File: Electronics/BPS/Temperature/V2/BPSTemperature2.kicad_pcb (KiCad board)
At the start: 2 copper layers, 75 x 65 mm, 81 parts, among them J1 Conn_02x10_Counter_Clockwise, J2 Logic Analyzer, J3 Conn_02x06_Counter_Clockwise, J4 Conn_02x06_Counter_Clockwise, J5 Conn_01x02, SW1 SW_DIP_x06, U1 LTC2983

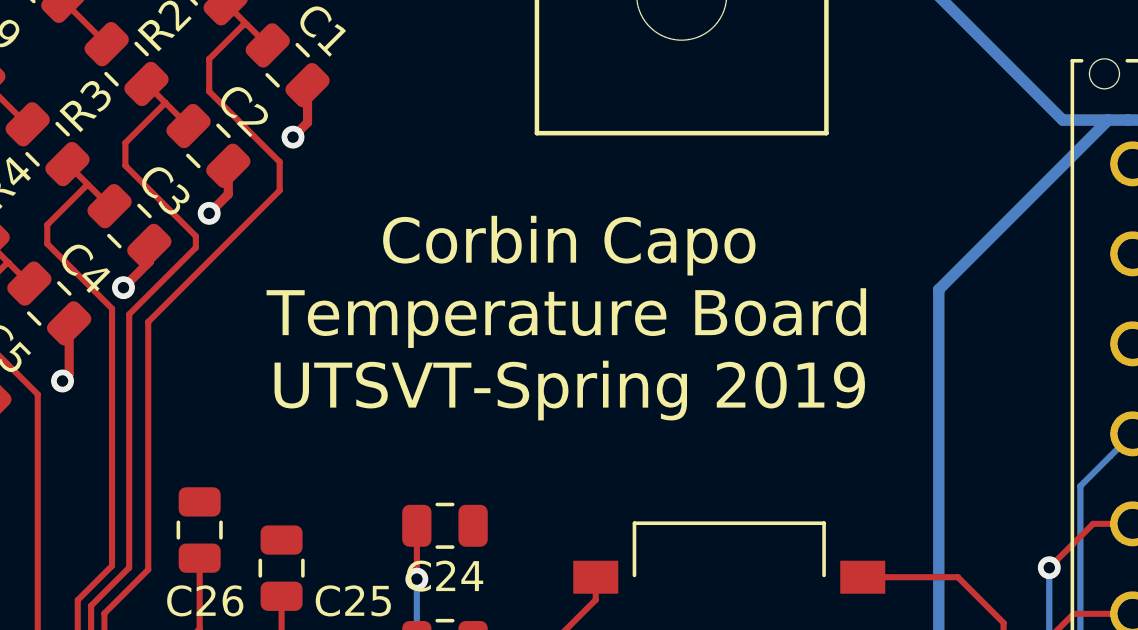
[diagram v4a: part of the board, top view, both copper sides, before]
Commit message: Added names to temperature board for BPS
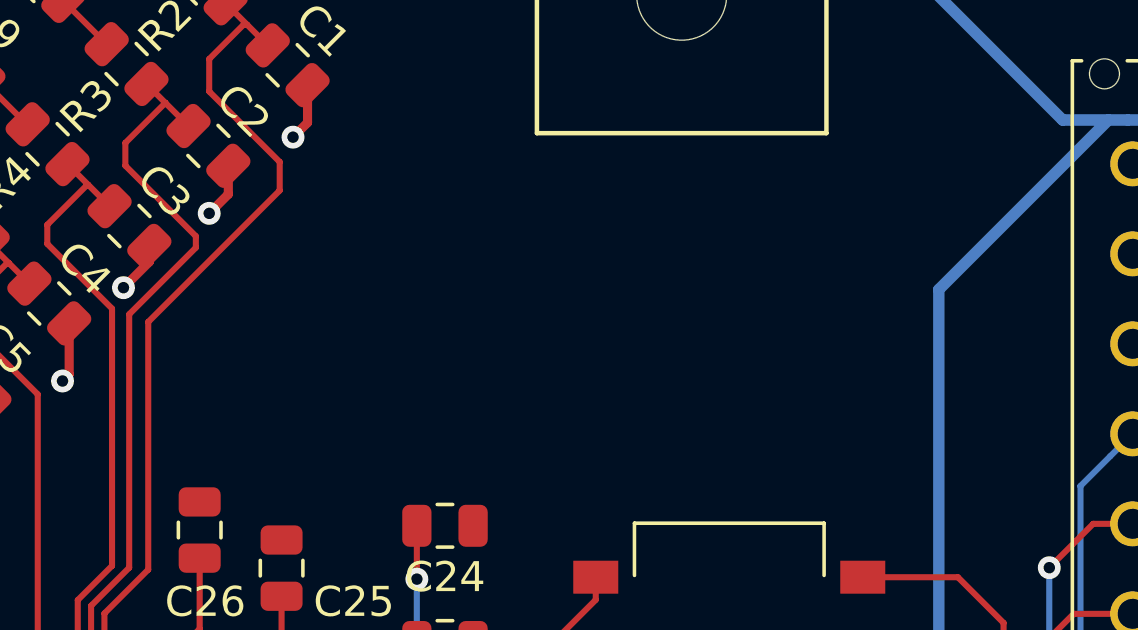
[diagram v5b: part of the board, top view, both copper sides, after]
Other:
- board text added: "Monolo Alvarez Chase Block Corbin Capo Richard Li Garrett Wong Sijin Woo Temperature Board UTSVT-Spring 2019"
- board text removed: "Corbin Capo Temperature Board UTSVT-Spring 2019"
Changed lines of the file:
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@@
     (effects (font (size 1.5 1.5) (thickness 0.3)))
   )
-  (gr_text "Corbin Capo\nTemperature Board\nUTSVT-Spring 2019" (at 109.601 86.5505) (layer F.SilkS)
-    (effects (font (size 1.5 1.5) (thickness 0.3)))
+  (gr_text "Monolo Alvarez\n\nChase Block\n\nCorbin Capo\n\nRichard Li\n\nGarrett Wong\n\nSijin Woo\nTemperature Board\nUTSVT-Spring 2019" (at 101.981 82.296) (layer B.SilkS)
+    (effects (font (size 0.738 0.738) (thickness 0.1845)) (justify mirror))
   )
   (gr_line (start 135 70) (end 60 70) (layer Edge.Cuts) (width 0.1))

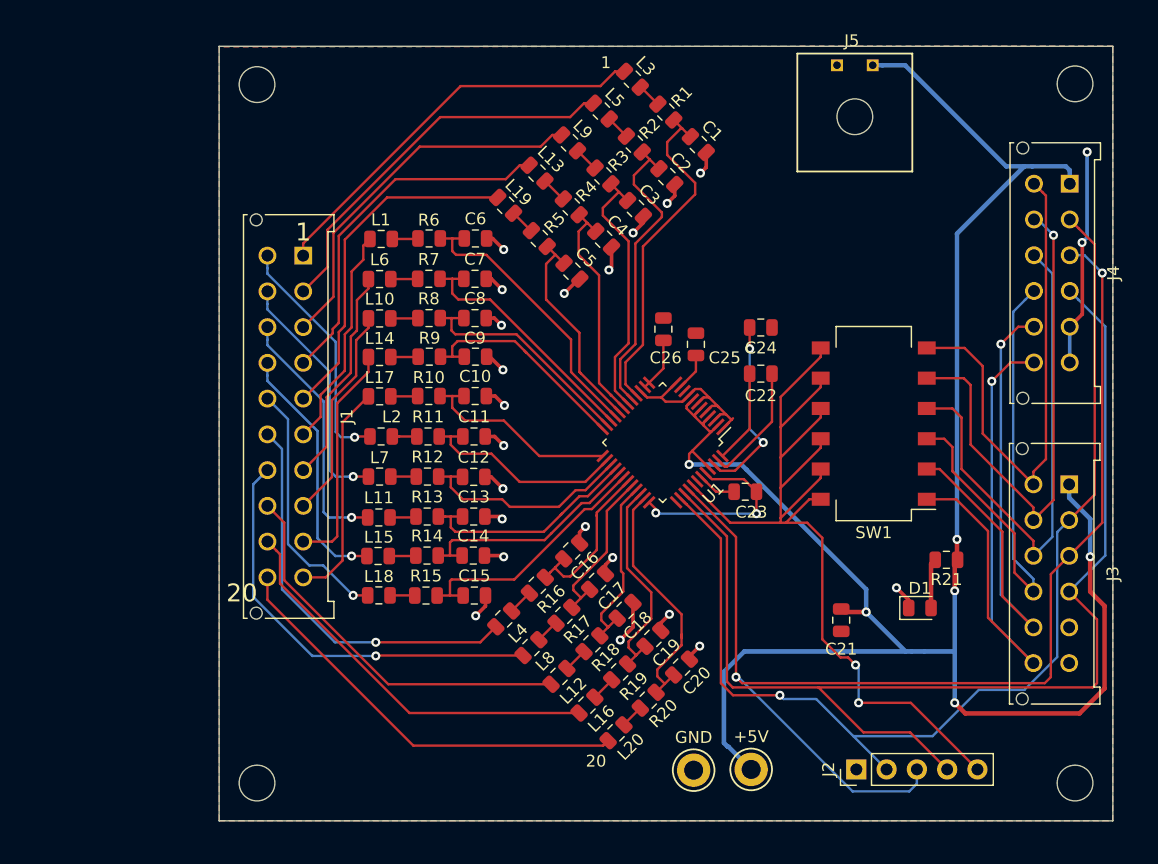
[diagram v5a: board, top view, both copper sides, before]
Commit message: Modified footprint for connector
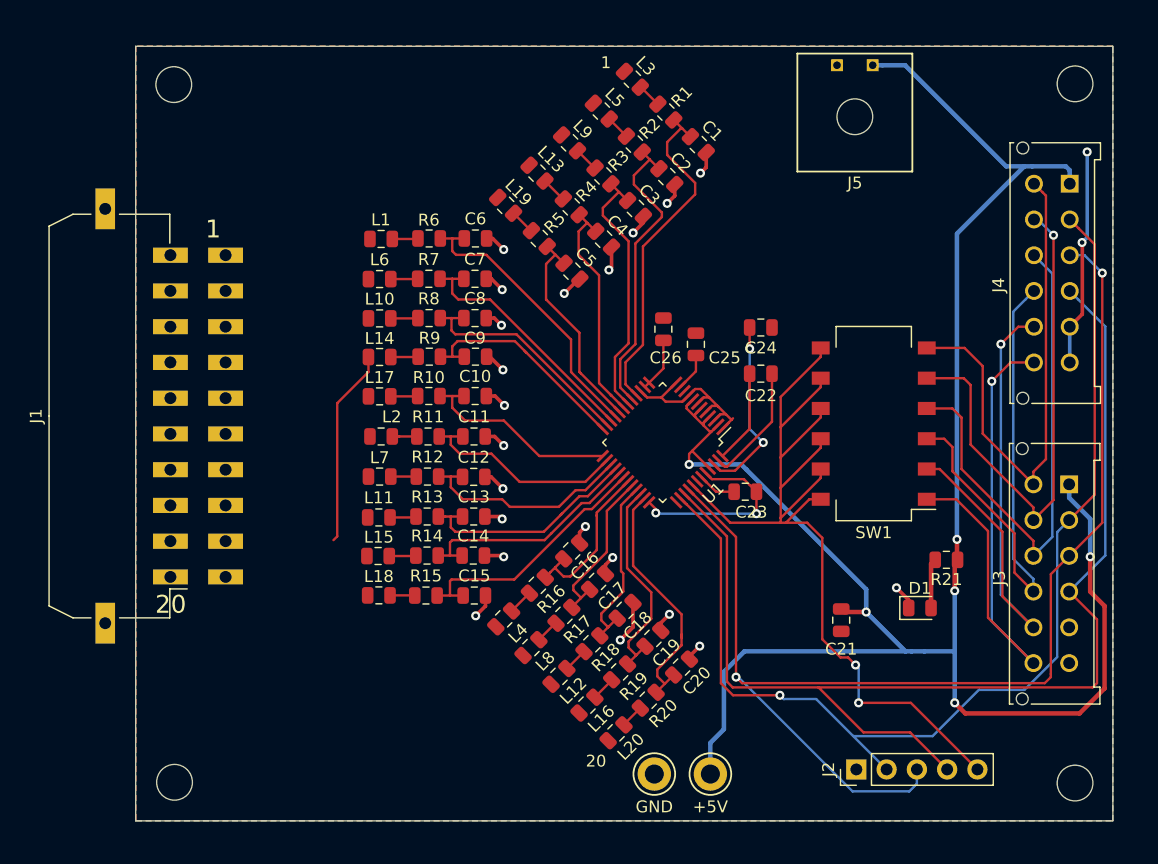
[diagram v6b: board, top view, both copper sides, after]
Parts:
- J1: footprint Connector_Molex:Molex_Micro-Fit_3.0_43045-2012_2x10_P3.00mm_Vertical -> UTSVT_Connectors:Molex_Micro-Fit_3.0_43045-2010_2x10-1MP_P3.00mm_Horizontal
- moved J1 16.1 mm to (58.2, 101.0), turned to 90 degrees
- moved MH1 6.98 mm to (56.2, 73.2)
- moved MH2 6.92 mm to (56.3, 131.8)
- moved +5V 3.44 mm to (101.2, 131.1), turned to 180 degrees
- moved GND 3.32 mm to (96.5, 131.1), turned to 180 degrees
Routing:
- net /CH17_LPF: track 35.8 -> 0.00 mm, vias 1 -> 0
- net /CH20_LPF: track 35.7 -> 0.00 mm
- net /CH1_LPF: track 34.0 -> 0.00 mm
- net /CH16_LPF: track 33.8 -> 0.00 mm, vias 1 -> 0
- net /CH19_LPF: track 33.6 -> 0.00 mm
- net /CH18_LPF: track 32.8 -> 0.00 mm
- net /CH2_LPF: track 32.7 -> 0.00 mm
- net /CH3_LPF: track 31.5 -> 0.00 mm
- net /CH4_LPF: track 30.3 -> 0.00 mm
- net /CH5_LPF: track 29.1 -> 0.00 mm
- net /CH15_LPF: track 21.4 -> 0.00 mm, vias 1 -> 0
- net /CH13_LPF: track 21.4 -> 0.00 mm, vias 1 -> 0
- net /CH14_LPF: track 21.2 -> 0.00 mm, vias 1 -> 0
- net /CH12_LPF: track 20.7 -> 0.00 mm, vias 1 -> 0
- net /CH11_LPF: track 20.3 -> 0.00 mm, vias 1 -> 0
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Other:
- board size 75 x 65 mm -> 82 x 65 mm

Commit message: Replaced connector footprint
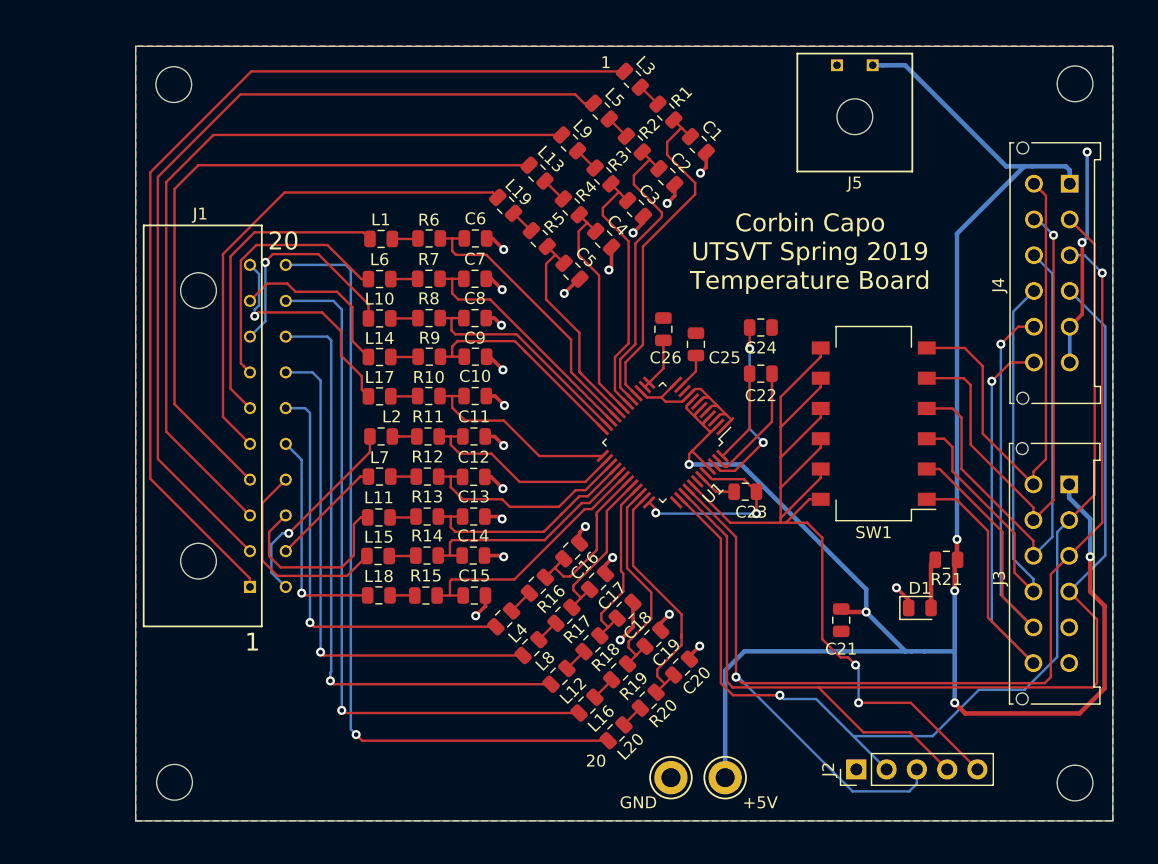
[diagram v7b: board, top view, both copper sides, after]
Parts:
- J1: footprint UTSVT_Connectors:Molex_Micro-Fit_3.0_43045-2010_2x10-1MP_P3.00mm_Horizontal -> UTSVT_Connectors:02x10_Microfit_3.0_horizontal
- moved J1 19.3 mm to (65.9, 118.7)
- moved GND 1.43 mm to (97.9, 131.4), turned to 0 degrees
- moved +5V 1.28 mm to (102.5, 131.4), turned to 0 degrees
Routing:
- net /CH1_LPF: track 0.00 -> 81.5 mm
- net /CH2_LPF: track 0.00 -> 74.3 mm
- net /CH20_LPF: track 0.00 -> 66.2 mm, vias 0 -> 1
- net /CH3_LPF: track 0.00 -> 65.7 mm
- net /CH19_LPF: track 0.00 -> 58.7 mm, vias 0 -> 1
- net /CH4_LPF: track 0.00 -> 57.6 mm
- net /CH18_LPF: track 0.00 -> 51.2 mm, vias 0 -> 1
- net /CH17_LPF: track 0.00 -> 43.1 mm, vias 0 -> 1
- net /CH5_LPF: track 0.00 -> 42.2 mm
- net /CH16_LPF: track 0.00 -> 35.5 mm, vias 0 -> 1
- net /CH6_LPF: track 0.00 -> 26.2 mm
- net /CH7_LPF: track 0.00 -> 22.1 mm
- net /CH10_LPF: track 0.00 -> 19.2 mm, vias 0 -> 1
- net /CH15_LPF: track 0.00 -> 18.7 mm, vias 0 -> 1
- net /CH8_LPF: track 0.00 -> 18.7 mm, vias 0 -> 1
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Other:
- board text added: "Corbin Capo UTSVT Spring 2019 Temperature Board"
- board text added: "Monolo Alvarez Chase Block Richard Li Garrett Wong Sijin Woo Temperature Board UTSVT-Spring 2019"
- board text removed: "Monolo Alvarez Chase Block Corbin Capo Richard Li Garrett Wong Sijin Woo Temperature Board UTSVT-Spring 2019"
